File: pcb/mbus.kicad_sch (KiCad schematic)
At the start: 25 parts, among them Q3 BSS84, Q5 Q_NPN_BEC_BRT, U3 MC33072, U4 LM4040DBZ-5

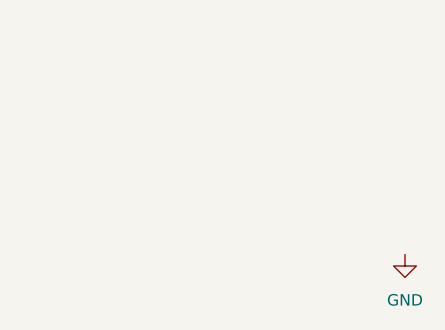
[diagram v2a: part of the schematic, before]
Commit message: * [0.1-dev] Add git commit references and README
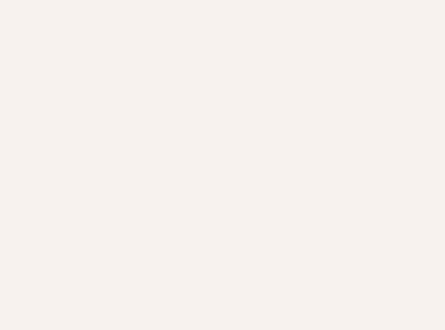
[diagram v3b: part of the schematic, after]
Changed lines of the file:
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@@
 (kicad_sch (version 20230121) (generator eeschema)
-  (paper "A4")
+  (paper "A3")
   (title_block
     (title "emonHP")
-    (date "2024-07-02")
-    (rev "0")
+    (date "2024-08-11")
+    (rev "0.1-dev")
     (company "Tilt Ltd / OpenEnergyMonitor")
+    (comment 1 "Creative Commons Attribution-ShareAlike 4.0 License")
+    (comment 2 "Commit: gitrev")
   )
   (junction (at 135.89 96.52) (diameter 0) (color 0 0 0 0)
@@
         )
       )
-    )
-  )
-  (symbol (lib_id "power:GND") (at 270.51 160.02 0) (unit 1)
-    (in_bom yes) (on_board yes) (dnp no) (fields_autoplaced)
-    (property "Reference" "#PWR022" (at 270.51 166.37 0)
-      (effects (font (size 1.27 1.27)) hide)
-    )
-    (property "Value" "GND" (at 270.51 165.1 0)
-      (effects (font (size 1.27 1.27)))
-    )
-    (property "Footprint" "" (at 270.51 160.02 0)
-      (effects (font (size 1.27 1.27)) hide)
-    )
-    (property "Datasheet" "" (at 270.51 160.02 0)
-      (effects (font (size 1.27 1.27)) hide)
-    )
-    (pin "1")
-    (instances
-      (project "mbus-reader-proto"
-        (path "/36d146b0-f348-4341-a935-471af0e684a6"
-          (reference "#PWR022") (unit 1)
-        )
-      )
-      (project "emonHP"
-        (path "/afefbb79-c2cc-4097-b792-3e37a295b6e5/47d3f211-4a48-4ab2-adbe-56046b34137e"
-          (reference "#PWR040") (unit 1)
-        )
-      )

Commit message: [v0.1-dev] First pass on emonPi format
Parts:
- Q?: renamed from Q3; value BSS84 -> FDN5618P
- U? (x3): renamed from U3; MPN (none) -> MC33072DR2G; Mouser (none) -> 863-MC33072DR2G
- U?: renamed from U4; MPN (none) -> LM4040DYM3-5.0-TR; Mouser (none) -> 998-LM4040DYM3-5.0TR
- renumbered C6 to C?, C3 to C?, D3 to D?, D2 to D?, Q5 to Q1, Q5 to Q3, R31 to R43, R32 to R44, R25 to R?, R24 to R?, R14 to R?, R21 to R?, R13 to R?, R18 to R?, R16 to R?, R17 to R?, R27 to R?, R12 to R?, R11 to R?, R9 to R?, R10 to R?, R15 to R?

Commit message: Swap 1Wire and AC sense
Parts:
- C?: LCSC (none) -> C307331
- D?: LCSC (none) -> C124196
- D?: LCSC (none) -> C5244698
- Q?: LCSC (none) -> C400792
- R43, R? (x3): LCSC (none) -> C25765
- R44, R? (x2): LCSC (none) -> C11702
- R? (x3): LCSC (none) -> C25741
- R? (x2): LCSC (none) -> C25760
- U? (x3): LCSC (none) -> C112613
- U?: LCSC (none) -> C156302
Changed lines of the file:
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@@
+      (effects (font (size 1.27 1.27)) hide)
+    )
+    (property "LCSC" "C11702" (at 168.91 111.76 90)
       (effects (font (size 1.27 1.27)) hide)
     )
@@
       (effects (font (size 1.27 1.27)) hide)
     )
+    (property "LCSC" "C25741" (at 116.84 139.7 0)
+      (effects (font (size 1.27 1.27)) hide)
+    )
     (pin "1")
     (pin "2")
@@
     )
     (property "Datasheet" "~" (at 124.46 92.71 0)
+      (effects (font (size 1.27 1.27)) hide)
+    )
+    (property "LCSC" "C25765" (at 124.46 92.71 90)
       (effects (font (size 1.27 1.27)) hide)
     )
@@
     )
     (property "Mouser" "863-MC33072DR2G" (at 151.13 99.06 0)
+      (effects (font (size 1.27 1.27)) hide)
+    )
+    (property "LCSC" "C112613" (at 151.13 99.06 0)
       (effects (font (size 1.27 1.27)) hide)
     )
@@
       (effects (font (size 1.27 1.27)) hide)
     )
+    (property "LCSC" "C156302" (at 142.24 139.7 90)
+      (effects (font (size 1.27 1.27)) hide)
+    )
     (pin "1")
     (pin "2")
@@
     )
     (property "Datasheet" "~" (at 186.69 102.87 0)
+      (effects (font (size 1.27 1.27)) hide)
+    )
+    (property "LCSC" "C25760" (at 186.69 102.87 90)
       (effects (font (size 1.27 1.27)) hide)
     )
@@
       (effects (font (size 1.27 1.27)) hide)
     )
+    (property "LCSC" "C25765" (at 151.13 127 0)
+      (effects (font (size 1.27 1.27)) hide)
+    )
     (pin "1")
     (pin "2")
@@
     )
     (property "Datasheet" "https://diotec.com/tl_files/diotec/files/pdf/datasheets/bzt52b2v4.pdf" (at 116.84 66.04 0)
+      (effects (font (size 1.27 1.27)) hide)
+    )
+    (property "LCSC" "C124196" (at 116.84 66.04 90)
       (effects (font (size 1.27 1.27)) hide)
     )
@@
       (effects (font (size 1.27 1.27)) hide)
     )
+    (property "LCSC" "C25760" (at 176.53 125.73 0)
+      (effects (font (size 1.27 1.27)) hide)
+    )
     (pin "1")
     (pin "2")
@@
       (effects (font (size 1.27 1.27)) hide)
     )
+    (property "LCSC" "C5244698" (at 116.84 83.82 90)
+      (effects (font (size 1.27 1.27)) hide)
+    )
     (pin "1")
     (pin "2")
@@
       (effects (font (size 1.27 1.27)) hide)
     )
+    (property "LCSC" "C25765" (at 124.46 105.41 90)
+      (effects (font (size 1.27 1.27)) hide)
+    )
     (pin "1")
     (pin "2")
@@
       (effects (font (size 1.27 1.27)) hide)
     )
+    (property "LCSC" "C25741" (at 135.89 111.76 0)
+      (effects (font (size 1.27 1.27)) hide)
+    )
     (pin "1")
     (pin "2")
@@
     )
     (property "Mouser" "863-MC33072DR2G" (at 179.07 73.66 0)
+      (effects (font (size 1.27 1.27)) hide)
+    )
+    (property "LCSC" "C112613" (at 179.07 73.66 0)
       (effects (font (size 1.27 1.27)) hide)
     )
@@
       (effects (font (size 1.27 1.27)))
     )
+    (property "LCSC" "C307331" (at 194.31 71.12 0)
+      (effects (font (size 1.27 1.27)) hide)
+    )
     (pin "1")
     (pin "2")
@@
       (effects (font (size 1.27 1.27)) hide)
     )
+    (property "LCSC" "C25765" (at 220.98 40.64 0)
+      (effects (font (size 1.27 1.27)) hide)
+    )
     (pin "1")
     (pin "2")
@@
       (effects (font (size 1.27 1.27)) hide)
     )
+    (property "LCSC" "C11702" (at 220.98 53.34 0)
+      (effects (font (size 1.27 1.27)) hide)
+    )
     (pin "1")
     (pin "2")
@@
     )
     (property "Datasheet" "~" (at 149.86 111.76 0)
+      (effects (font (size 1.27 1.27)) hide)
+    )
+    (property "LCSC" "C25741" (at 149.86 111.76 90)
       (effects (font (size 1.27 1.27)) hide)
     )
@@
     )
     (property "Mouser" "863-MC33072DR2G" (at 187.96 115.57 0)
+      (effects (font (size 1.27 1.27)) hide)
+    )
+    (property "LCSC" "C112613" (at 187.96 115.57 0)
       (effects (font (size 1.27 1.27)) hide)
     )
@@
       (effects (font (size 1.27 1.27)) hide)
     )
+    (property "LCSC" "C11702" (at 168.91 119.38 90)
+      (effects (font (size 1.27 1.27)) hide)
+    )
     (pin "1")
     (pin "2")
@@
       (effects (font (size 1.27 1.27)) (justify left) hide)
     )
-    (pin "1")
+    (property "LCSC" "C400792" (at 66.04 69.85 0)
+      (effects (font (size 1.27 1.27)) hide)
+    )
+    (pin "1")
